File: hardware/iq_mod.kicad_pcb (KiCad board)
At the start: 4 copper layers, 100 x 100 mm, 186 parts, among them J1001 USB-C, J101 SMA, J102 SMA, J103 SMA, J104 SMA, J1101 SMA, J1102 SMA, J1103 SMA, J201 SMA, J202 SMA, J203 SMA, J204 SMA, J301 SMA, J302 SMA, J303 SMA, J304 Pmod, J401 SMA, J402 SMA, J501 SMA, J502 SMA, J503 SMA, J504 SMA, J601 SMA, J602 SMA, J701 SMA, J801 SMA, J802 SMA, J901 SMA, J902 SMA, Q101 AO3401A, Q201 AO3401A, Q301 AO3401A, Q401 AO3401A, Q601 AO3401A, Q701 AO3401A, Q702 MMBT3904, Q801 AO3401A, SW101 ON, SW201 ON, SW301 ON, SW401 ON, SW601 ON, SW701 ON, SW801 ON, U1001 LM2664, U101 ADL5375, U1101 SKY13370, U201 ADL5380, U202 OPA810, U203 OPA810, U301 3.3V, U302 MAX2871, U401 QPL9547, U501 HHM22137A1, U502 HHM22137A1, U601 AD8318, U701 TPS22917, U702 ADL5611, U801 MAX2659, U802 3.3V

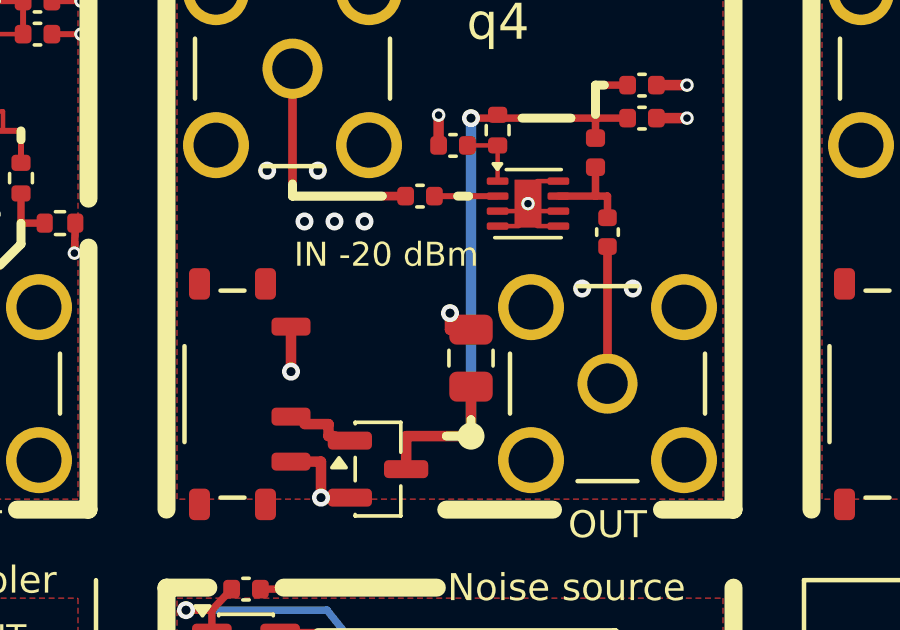
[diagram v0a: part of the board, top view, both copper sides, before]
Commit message: Pre-order checks from CLAUDE_PCB.md's new lessons (Prompt 21): the KF301 terminals turned for their wire openings (CPL +180, body 3.7 / 4.0, a wire-face check), four oversold parts swapped (27R, 6.8k, 220n, OPA847IDBVT at its own +180), fourteen vias moved out of SMD pads (check_layout.py gates it and RF detours), 200-250 mW terminations, assembly drawings from Fab and silk fitted to Letter (fit_pdf.py from CostasLink), the stock gate on JLCPCB's free count, electrolytics in the rotation check, the RF gates surveyed (rf_extract.py, rf_survey.py) and written into the DOA lists; all nine boards rebuilt: ERC 0, DRC 0, every check
Co-Authored-By: Claude Opus 5.5 <noreply@anthropic.com>
Claude-Session: https://claude.ai/code/session_01RKeoKvFFzjk3cEBLCXXHnB
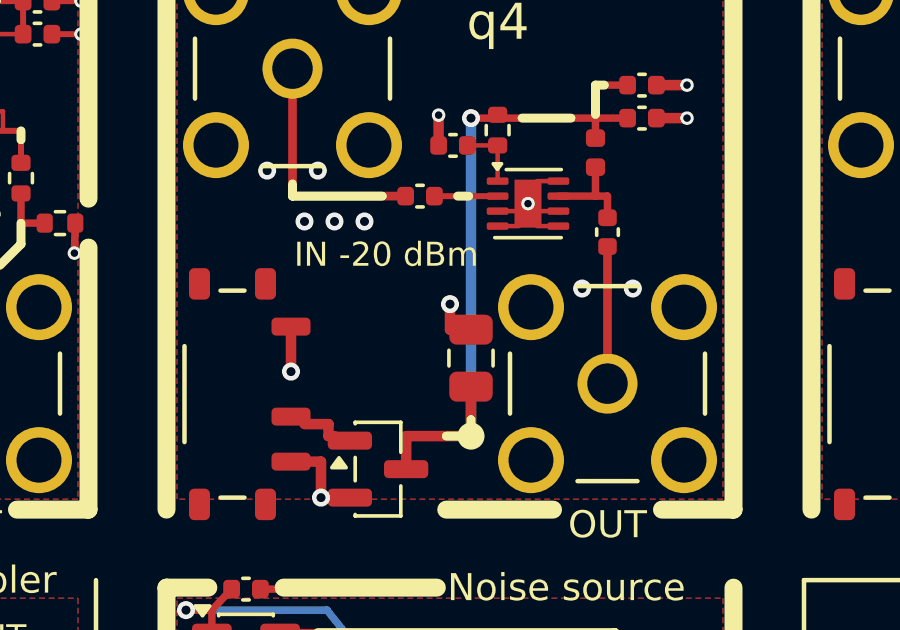
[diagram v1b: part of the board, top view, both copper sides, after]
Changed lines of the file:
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@@
 			)
 		)
-		(property "LCSC" "C25120"
+		(property "LCSC" "C844112"
 			(at 0 0 270)
 			(layer "F.Fab")
@@
 			)
 		)
-		(property "MPN" "0402WGF499JTCE"
+		(property "MPN" "CRCW040249R9FKEDHP"
 			(at 0 0 270)
 			(layer "F.Fab")
@@
 			)
 		)
-		(property "LCSC" "C25120"
+		(property "LCSC" "C844112"
 			(at 0 0 90)
 			(layer "F.Fab")
@@
 			)
 		)
-		(property "MPN" "0402WGF499JTCE"
+		(property "MPN" "CRCW040249R9FKEDHP"
 			(at 0 0 90)
 			(layer "F.Fab")
@@
 	)
 	(segment
+		(start 60.75 21.2)
+		(end 60.75 20.35)
+		(width 0.35)
+		(layer "F.Cu")
+		(net "GND")
+	)
+	(segment
 		(start 42.925 16.2)
 		(end 42.925 15.25)
@@
 	)
 	(segment
-		(start 60.75 21.2)
-		(end 60.75 20.65)
-		(width 0.35)
-		(layer "F.Cu")
-		(net "GND")
-	)
-	(segment
 		(start 70.4 61)
 		(end 71.25 61)
@@
 	)
 	(via
-		(at 60.75 20.65)
-		(size 0.6)
-		(drill 0.3)
-		(layers "F.Cu" "B.Cu")
-		(tenting
-			(front yes)
-			(back yes)
-		)
-		(net "GND")
-	)
-	(via
 		(at 55.35 29.85)
 		(size 0.45)
@@
 		(layers "F.Cu" "B.Cu")
 		(tenting
+			(front yes)
+			(back yes)
+		)
+		(net "GND")
+	)
+	(via
+		(at 60.75 20.35)
+		(size 0.6)
+		(drill 0.3)
+		(layers "F.Cu" "B.Cu")
+		(tenting
